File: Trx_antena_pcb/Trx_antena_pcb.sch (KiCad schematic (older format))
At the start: 3 parts

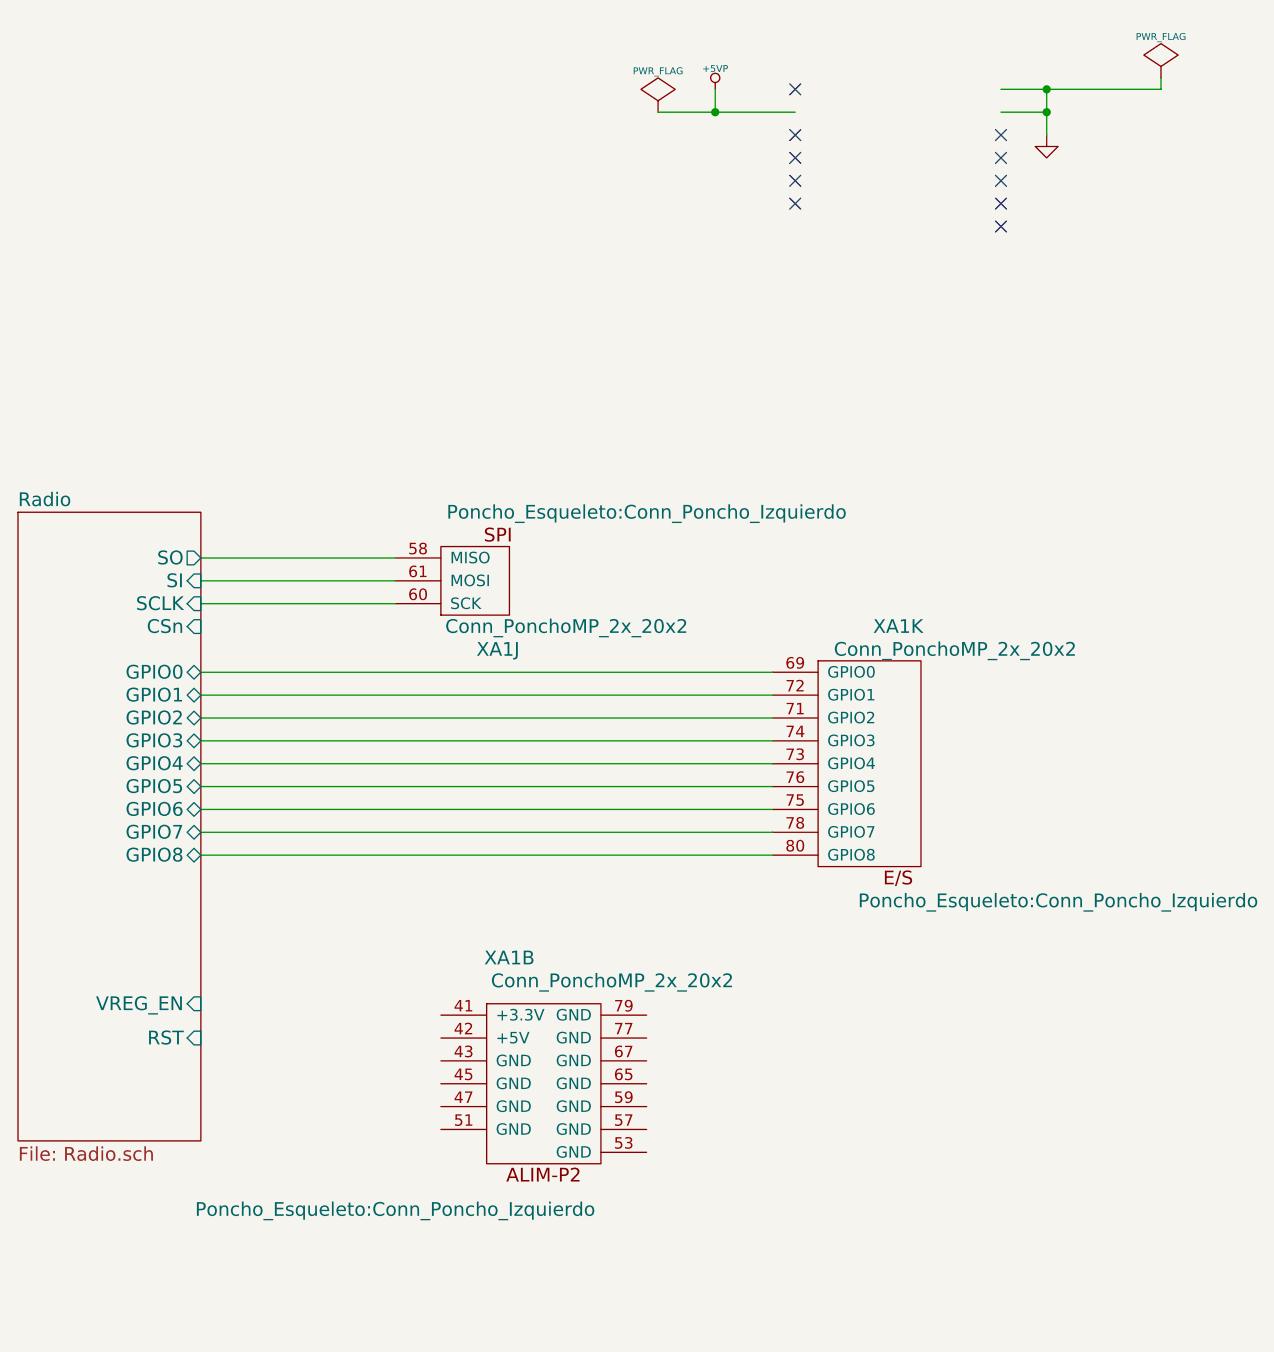
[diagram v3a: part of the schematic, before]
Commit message: completando el esquematico
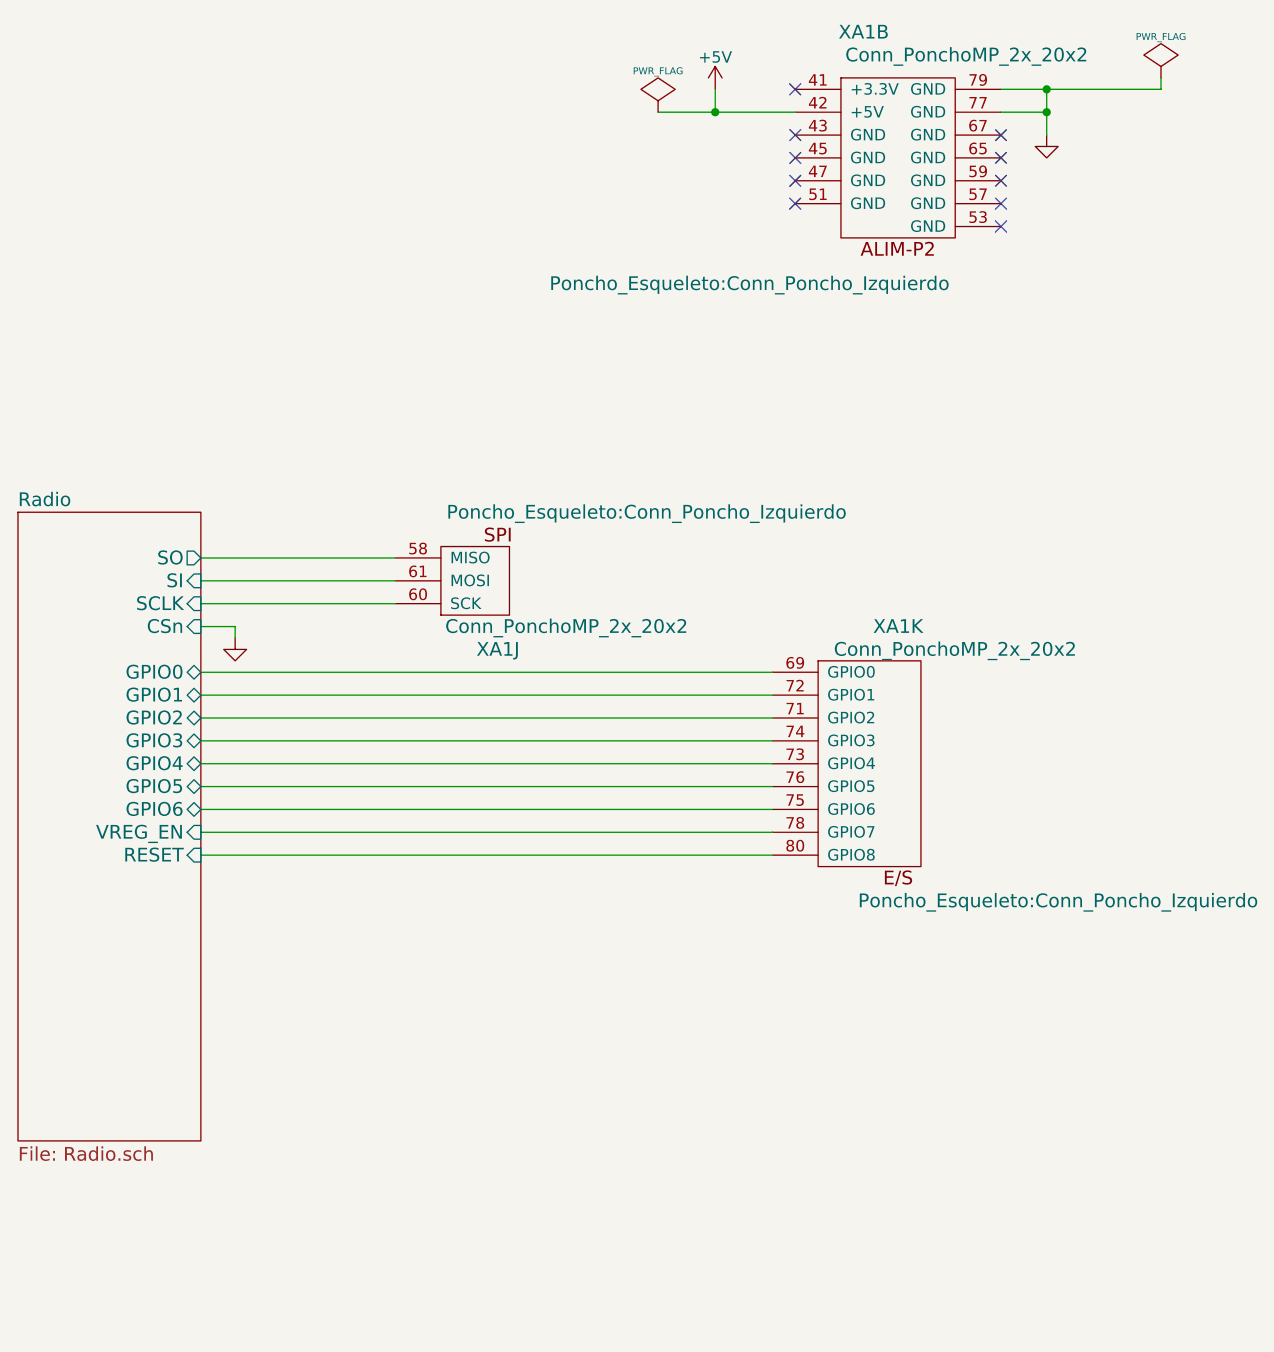
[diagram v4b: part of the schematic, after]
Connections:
- net labels added: +5V
- net labels removed: +5VP
- wire segments 18 -> 20
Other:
- moved on the sheet: XA1B
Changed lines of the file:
@@
 $EndComp
 $Comp
-L PWR_FLAG #FLG1
+L PWR_FLAG #FLG01
 U 1 1 560EE826
 P 3750 1050
-F 0 "#FLG1" H 3750 1145 30  0001 C CNN
+F 0 "#FLG01" H 3750 1145 30  0001 C CNN
 F 1 "PWR_FLAG" H 3750 1230 30  0000 C CNN
 F 2 "" H 3750 1050 60  0000 C CNN
@@
 $EndComp
 $Comp
-L +5VP #PWR2
-U 1 1 560EE7D3
-P 4000 950
-F 0 "#PWR2" H 4000 1040 20  0001 C CNN
-F 1 "+5VP" H 4000 1040 30  0000 C CNN
-F 2 "" H 4000 950 60  0000 C CNN
-F 3 "" H 4000 950 60  0000 C CNN
-	1    4000 950
-	1    0    0    -1
-$EndComp
-$Comp
-L GND #PWR5
+L GND #PWR02
 U 1 1 560EE345
 P 5450 1150
-F 0 "#PWR5" H 5450 1150 30  0001 C CNN
+F 0 "#PWR02" H 5450 1150 30  0001 C CNN
 F 1 "GND" H 5450 1080 30  0001 C CNN
 F 2 "" H 5450 1150 60  0000 C CNN
@@
 L Conn_PonchoMP_2x_20x2 XA1
 U 2 1 560EE110
-P 3250 5300
-F 0 "XA1" H 3100 5850 60  0000 C CNN
-F 1 "Conn_PonchoMP_2x_20x2" H 3550 5750 60  0000 C CNN
-F 2 "Poncho_Esqueleto:Conn_Poncho_Izquierdo" H 2600 4750 60  0000 C CNN
-F 3 "" H 3100 5650 60  0000 C CNN
-	2    3250 5300
+P 4800 1250
+F 0 "XA1" H 4650 1800 60  0000 C CNN
+F 1 "Conn_PonchoMP_2x_20x2" H 5100 1700 60  0000 C CNN
+F 2 "Poncho_Esqueleto:Conn_Poncho_Izquierdo" H 4150 700 60  0000 C CNN
+F 3 "" H 4650 1600 60  0000 C CNN
+	2    4800 1250
 	1    0    0    -1
 $EndComp
 $Comp
-L PWR_FLAG #FLG2
+L PWR_FLAG #FLG03
 U 1 1 560EDE73
 P 5950 900
-F 0 "#FLG2" H 5950 995 30  0001 C CNN
+F 0 "#FLG03" H 5950 995 30  0001 C CNN
 F 1 "PWR_FLAG" H 5950 1080 30  0000 C CNN
 F 2 "" H 5950 900 60  0000 C CNN
@@
 Text Notes 7450 5650 0    60   ~ 0
 Agujeros para visualización de LEDs
-$Sheet
-S 950  2800 800  2750
-U 582F8126
-F0 "Radio" 60
-F1 "Radio.sch" 60
-F2 "SO" O R 1750 3000 60
-F3 "SI" I R 1750 3100 60
-F4 "VREG_EN" I R 1750 4950 60
-F5 "SCLK" I R 1750 3200 60
-F6 "GPIO0" B R 1750 3500 60
-F7 "GPIO1" B R 1750 3600 60
-F8 "GPIO2" B R 1750 3700 60
-F9 "GPIO3" B R 1750 3800 60
-F10 "GPIO4" B R 1750 3900 60
-F11 "GPIO5" B R 1750 4000 60
-F12 "RST" I R 1750 5100 60
-F13 "CSn" I R 1750 3300 60
-F14 "GPIO6" B R 1750 4100 60
-F15 "GPIO7" B R 1750 4200 60
-F16 "GPIO8" B R 1750 4300 60
-$EndSheet
 Connection ~ 4000 1050
 Wire Wire Line
@@
 Wire Wire Line
 	1750 4100 4250 4100
+$Sheet
+S 950  2800 800  2750
+U 582F8126
+F0 "Radio" 60
+F1 "Radio.sch" 60
+F2 "SO" O R 1750 3000 60
+F3 "SI" I R 1750 3100 60
+F4 "VREG_EN" I R 1750 4200 60
+F5 "SCLK" I R 1750 3200 60
+F6 "GPIO0" B R 1750 3500 60
+F7 "GPIO1" B R 1750 3600 60
+F8 "GPIO2" B R 1750 3700 60
+F9 "GPIO3" B R 1750 3800 60
+F10 "GPIO4" B R 1750 3900 60
+F11 "GPIO5" B R 1750 4000 60
+F12 "CSn" I R 1750 3300 60
+F13 "GPIO6" B R 1750 4100 60
+F14 "RESET" I R 1750 4300 60
+$EndSheet
 Wire Wire Line
-	1750 4200 4250 4200
+	4250 4200 1750 4200
+$Comp
+L +5V #PWR04
+U 1 1 5851A27B
+P 4000 950
+F 0 "#PWR04" H 4000 800 50  0001 C CNN
+F 1 "+5V" H 4000 1090 50  0000 C CNN
+F 2 "" H 4000 950 50  0000 C CNN
+F 3 "" H 4000 950 50  0000 C CNN
+	1    4000 950
+	1    0    0    -1
+$EndComp
 Wire Wire Line
-	1750 4300 4250 4300
+	4250 4300 1750 4300
+$Comp
+L GND #PWR05
+U 1 1 5852BF25
+P 1900 3350
+F 0 "#PWR05" H 1900 3350 30  0001 C CNN
+F 1 "GND" H 1900 3280 30  0001 C CNN
+F 2 "" H 1900 3350 60  0000 C CNN
+F 3 "" H 1900 3350 60  0000 C CNN
+	1    1900 3350
+	1    0    0    -1
+$EndComp
+Wire Wire Line
+	1900 3350 1900 3300
+Wire Wire Line
+	1900 3300 1750 3300
 $EndSCHEMATC

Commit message: cuarta correccion: revision2 en /doc
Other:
- note added: "Este circuito de poncho implementa una unidad de radio \nque opera en la banda de frecuencias abierta de 2.4GHz \ny compila con aplicaciones de la EDU-CIAA NXP \nque soportan el estándar IEEE 802.15.4: IEEE Standards Association. \nIEEE Standard for Local and metropolitan area networks–Part 15.4: \nLow-Rate Wireless Personal Area Networks (LR-WPANs) y ZIGBEE.\n\n2.4 GHz Antena(DN007): Inverted-F 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"
- note removed: "Este diseño puede copiarse como un \nTemplate de KICAD. \n1)En el administrador de Proyectos: \n Proyecto Nuevo -> Nuevo Proyecto desde Template\n2)Ingresar el nombre del poncho a crear.\n3)Indicar el directorio de este modelo."
- note removed: "Luego de abrir el nuevo proyecto:\n1)Editar datos del rótulo.\n2)Editar los archivos del subdirectorio "doc".\n2.1) Agregarse en el archivo de licencia.\n2.2) Colocar info mínima del Poncho en el LEEME.txt\n2.3) Colocar info mínima en el CAMBIOS.doc"
- moved on the sheet: XA1B, XA1J, XA1K
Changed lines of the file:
@@
 EESchema Schematic File Version 2
-LIBS:device
+LIBS:power
 LIBS:Trx_antena_pcb-cache
 EELAYER 25 0
@@
 Comment1 "https://github.com/ciaa/Ponchos/tree/master/modelos/doc"
 Comment2 "Basado en el template de Diego Brengi - UNLaM"
-Comment3 "Autor y Licencia del poncho (Juan Vicente Montilla-FIUBA). Ver directorio \"doc\""
-Comment4 "https://github.com/Juanvmont/Poncho-EDU-CIAA-NXP-RF-2.4GHz-Antena-PCB.git"
+Comment3 "Revisor designado (Esp. Ing. Patricio Bos-FIUBA)."
+Comment4 "Autor y Licencia del poncho (Esp. Ing. Juan Vicente Montilla-FIUBA). Ver directorio \"doc\""
 $EndDescr
 $Comp
@@
 	1    0    0    -1
 $EndComp
-Text Notes 6950 2850 0    79   Italic 16
-Este diseño puede copiarse como un \nTemplate de KICAD. \n1)En el administrador de Proyectos:  \n   Proyecto Nuevo -> Nuevo Proyecto desde Template\n2)Ingresar el nombre del poncho a crear.\n3)Indicar el directorio de este modelo.
-Text Notes 7000 1800 0    118  ~ 24
+Text Notes 7800 900  0    118  ~ 24
 http://www.proyecto-ciaa.com.ar/
 $Comp
 L Conn_PonchoMP_2x_20x2 XA1
 U 11 1 560E5596
-P 4700 3800
-F 0 "XA1" H 4600 4300 60  0000 C CNN
-F 1 "Conn_PonchoMP_2x_20x2" H 4350 4200 60  0000 C CNN
-F 2 "Poncho_Esqueleto:Conn_Poncho_Izquierdo" H 3900 3100 60  0000 C CNN
-F 3 "" H 4550 4150 60  0000 C CNN
-	11   4700 3800
+P 7100 2700
+F 0 "XA1" H 7000 3200 60  0000 C CNN
+F 1 "Conn_PonchoMP_2x_20x2" H 6750 3100 60  0000 C CNN
+F 2 "Poncho_Esqueleto:Conn_Poncho_Izquierdo" H 6300 2000 60  0001 C CNN
+F 3 "" H 6950 3050 60  0000 C CNN
+	11   7100 2700
 	-1   0    0    -1
 $EndComp
-Text Notes 7000 3950 0    60   ~ 0
-Luego de abrir el nuevo proyecto:\n1)Editar datos del rótulo.\n2)Editar los archivos del subdirectorio "doc".\n2.1) Agregarse en el archivo de licencia.\n2.2) Colocar info mínima del Poncho en el LEEME.txt\n2.3) Colocar info mínima en el CAMBIOS.doc
 $Comp
 L Conn_PonchoMP_2x_20x2 XA1
 U 10 1 560E54EF
-P 2950 3100
-F 0 "XA1" H 2850 3400 60  0000 C CNN
-F 1 "Conn_PonchoMP_2x_20x2" H 2550 3300 60  0000 C CNN
-F 2 "Poncho_Esqueleto:Conn_Poncho_Izquierdo" H 2200 2800 60  0000 C CNN
-F 3 "" H 2800 3450 60  0000 C CNN
-	10   2950 3100
+P 5350 2000
+F 0 "XA1" H 5250 2300 60  0000 C CNN
+F 1 "Conn_PonchoMP_2x_20x2" H 4950 2200 60  0000 C CNN
+F 2 "Poncho_Esqueleto:Conn_Poncho_Izquierdo" H 4600 1700 60  0001 C CNN
+F 3 "" H 5200 2350 60  0000 C CNN
+	10   5350 2000
 	-1   0    0    1
 $EndComp
@@
 L PWR_FLAG #FLG01
 U 1 1 560EE826
-P 3750 1050
-F 0 "#FLG01" H 3750 1145 30  0001 C CNN
-F 1 "PWR_FLAG" H 3750 1230 30  0000 C CNN
-F 2 "" H 3750 1050 60  0000 C CNN
-F 3 "" H 3750 1050 60  0000 C CNN
-	1    3750 1050
+P 5100 4350
+F 0 "#FLG01" H 5100 4445 30  0001 C CNN
+F 1 "PWR_FLAG" H 5100 4530 30  0000 C CNN
+F 2 "" H 5100 4350 60  0000 C CNN
+F 3 "" H 5100 4350 60  0000 C CNN
+	1    5100 4350
 	1    0    0    -1
 $EndComp
@@
 L GND #PWR02
 U 1 1 560EE345
-P 5450 1150
-F 0 "#PWR02" H 5450 1150 30  0001 C CNN
-F 1 "GND" H 5450 1080 30  0001 C CNN
-F 2 "" H 5450 1150 60  0000 C CNN
-F 3 "" H 5450 1150 60  0000 C CNN
-	1    5450 1150
-	1    0    0    -1
-$EndComp
-NoConn ~ 5250 1150
-NoConn ~ 5250 1250
-NoConn ~ 5250 1350
-NoConn ~ 5250 1450
-NoConn ~ 5250 1550
-NoConn ~ 4350 1450
-NoConn ~ 4350 950
+P 6800 4450
+F 0 "#PWR02" H 6800 4450 30  0001 C CNN
+F 1 "GND" H 6800 4380 30  0001 C CNN
+F 2 "" H 6800 4450 60  0000 C CNN
+F 3 "" H 6800 4450 60  0000 C CNN
+	1    6800 4450
+	1    0    0    -1
+$EndComp
+NoConn ~ 6600 4450
+NoConn ~ 6600 4550
+NoConn ~ 6600 4650
+NoConn ~ 6600 4750
+NoConn ~ 6600 4850
+NoConn ~ 5700 4750
+NoConn ~ 5700 4250
 $Comp
 L Conn_PonchoMP_2x_20x2 XA1
 U 2 1 560EE110
-P 4800 1250
-F 0 "XA1" H 4650 1800 60  0000 C CNN
-F 1 "Conn_PonchoMP_2x_20x2" H 5100 1700 60  0000 C CNN
-F 2 "Poncho_Esqueleto:Conn_Poncho_Izquierdo" H 4150 700 60  0000 C CNN
-F 3 "" H 4650 1600 60  0000 C CNN
-	2    4800 1250
+P 6150 4550
+F 0 "XA1" H 6000 5100 60  0000 C CNN
+F 1 "Conn_PonchoMP_2x_20x2" H 6450 5000 60  0000 C CNN
+F 2 "Poncho_Esqueleto:Conn_Poncho_Izquierdo" H 5500 4000 60  0001 C CNN
+F 3 "" H 6000 4900 60  0000 C CNN
+	2    6150 4550
 	1    0    0    -1
 $EndComp
@@
 L PWR_FLAG #FLG03
 U 1 1 560EDE73
-P 5950 900
-F 0 "#FLG03" H 5950 995 30  0001 C CNN
-F 1 "PWR_FLAG" H 5950 1080 30  0000 C CNN
-F 2 "" H 5950 900 60  0000 C CNN
-F 3 "" H 5950 900 60  0000 C CNN
-	1    5950 900
-	1    0    0    -1
-$EndComp
-NoConn ~ 4350 1350
-NoConn ~ 4350 1250
-NoConn ~ 4350 1150
+P 7300 4200
+F 0 "#FLG03" H 7300 4295 30  0001 C CNN
+F 1 "PWR_FLAG" H 7300 4380 30  0000 C CNN
+F 2 "" H 7300 4200 60  0000 C CNN
+F 3 "" H 7300 4200 60  0000 C CNN
+	1    7300 4200
+	1    0    0    -1
+$EndComp
+NoConn ~ 5700 4650
+NoConn ~ 5700 4550
+NoConn ~ 5700 4450
 $Comp
 L PCB_HOLE H2
@@
 Text Notes 7450 5650 0    60   ~ 0
 Agujeros para visualización de LEDs
-Connection ~ 4000 1050
-Wire Wire Line
-	4000 1050 4000 950
-Wire Wire Line
-	3750 1050 4350 1050
-Connection ~ 5450 1050
-Wire Wire Line
-	5250 950  5950 950
-Wire Wire Line
-	5450 950  5450 1150
-Wire Wire Line
-	5250 1050 5450 1050
-Wire Wire Line
-	5950 950  5950 900
-Connection ~ 5450 950
-Wire Wire Line
-	2600 3000 1750 3000
-Wire Wire Line
-	2600 3100 1750 3100
-Wire Wire Line
-	2600 3200 1750 3200
-Wire Wire Line
-	1750 3500 4250 3500
-Wire Wire Line
-	4250 3600 1750 3600
-Wire Wire Line
-	1750 3700 4250 3700
-Wire Wire Line
-	1750 3800 4250 3800
-Wire Wire Line
-	1750 3900 4250 3900
-Wire Wire Line
-	1750 4000 4250 4000
-Wire Wire Line
-	1750 4100 4250 4100
+Connection ~ 5350 4350
+Wire Wire Line
+	5350 4350 5350 4250
+Wire Wire Line
+	5100 4350 5700 4350
+Connection ~ 6800 4350
+Wire Wire Line
+	6600 4250 7300 4250
+Wire Wire Line
+	6800 4250 6800 4450
+Wire Wire Line
+	6600 4350 6800 4350
+Wire Wire Line
+	7300 4250 7300 4200
+Connection ~ 6800 4250
+Wire Wire Line
+	5000 1900 4150 1900
+Wire Wire Line
+	5000 2000 4150 2000
+Wire Wire Line
+	5000 2100 4150 2100
+Wire Wire Line
+	4150 2400 6650 2400
+Wire Wire Line
+	6650 2500 4150 2500
+Wire Wire Line
+	4150 2600 6650 2600
+Wire Wire Line
+	4150 2700 6650 2700
+Wire Wire Line
+	4150 2800 6650 2800
+Wire Wire Line
+	4150 2900 6650 2900
+Wire Wire Line
+	4150 3000 6650 3000
 $Sheet
-S 950  2800 800  2750
+S 3350 1700 800  2750
 U 582F8126
 F0 "Radio" 60
 F1 "Radio.sch" 60
-F2 "SO" O R 1750 3000 60
-F3 "SI" I R 1750 3100 60
-F4 "VREG_EN" I R 1750 4200 60
-F5 "SCLK" I R 1750 3200 60
-F6 "GPIO0" B R 1750 3500 60
-F7 "GPIO1" B R 1750 3600 60
-F8 "GPIO2" B R 1750 3700 60
-F9 "GPIO3" B R 1750 3800 60
-F10 "GPIO4" B R 1750 3900 60
-F11 "GPIO5" B R 1750 4000 60
-F12 "CSn" I R 1750 3300 60
-F13 "GPIO6" B R 1750 4100 60
-F14 "RESET" I R 1750 4300 60
+F2 "SO" O R 4150 1900 60
+F3 "SI" I R 4150 2000 60
+F4 "VREG_EN" I R 4150 3100 60
+F5 "SCLK" I R 4150 2100 60
+F6 "GPIO0" B R 4150 2400 60
+F7 "GPIO1" B R 4150 2500 60
+F8 "GPIO2" B R 4150 2600 60
+F9 "GPIO3" B R 4150 2700 60
+F10 "GPIO4" B R 4150 2800 60
+F11 "GPIO5" B R 4150 2900 60
+F12 "CSn" I R 4150 2200 60
+F13 "GPIO6" B R 4150 3000 60
+F14 "RESET" I R 4150 3200 60
 $EndSheet
 Wire Wire Line
-	4250 4200 1750 4200
+	6650 3100 4150 3100
 $Comp
 L +5V #PWR04
 U 1 1 5851A27B
-P 4000 950
-F 0 "#PWR04" H 4000 800 50  0001 C CNN
-F 1 "+5V" H 4000 1090 50  0000 C CNN
-F 2 "" H 4000 950 50  0000 C CNN
-F 3 "" H 4000 950 50  0000 C CNN
-	1    4000 950
-	1    0    0    -1
-$EndComp
-Wire Wire Line
-	4250 4300 1750 4300
+P 5350 4250
+F 0 "#PWR04" H 5350 4100 50  0001 C CNN
+F 1 "+5V" H 5350 4390 50  0000 C CNN
+F 2 "" H 5350 4250 50  0000 C CNN
+F 3 "" H 5350 4250 50  0000 C CNN
+	1    5350 4250
+	1    0    0    -1
+$EndComp
+Wire Wire Line
+	6650 3200 4150 3200
 $Comp
 L GND #PWR05
 U 1 1 5852BF25
-P 1900 3350
-F 0 "#PWR05" H 1900 3350 30  0001 C CNN
-F 1 "GND" H 1900 3280 30  0001 C CNN
-F 2 "" H 1900 3350 60  0000 C CNN
-F 3 "" H 1900 3350 60  0000 C CNN
-	1    1900 3350
-	1    0    0    -1
-$EndComp
-Wire Wire Line
-	1900 3350 1900 3300
-Wire Wire Line
-	1900 3300 1750 3300
+P 4300 2250
+F 0 "#PWR05" H 4300 2250 30  0001 C CNN
+F 1 "GND" H 4300 2180 30  0001 C CNN
+F 2 "" H 4300 2250 60  0000 C CNN
+F 3 "" H 4300 2250 60  0000 C CNN
+	1    4300 2250
+	1    0    0    -1
+$EndComp
+Wire Wire Line
+	4300 2250 4300 2200
+Wire Wire Line
+	4300 2200 4150 2200
+Text Notes 1000 7200 0    60   ~ 0
+Este circuito de poncho implementa una unidad de radio \nque opera en la banda de frecuencias abierta de 2.4GHz \ny compila con aplicaciones de la EDU-CIAA NXP \nque soportan el estándar IEEE 802.15.4: IEEE Standards Association. \nIEEE Standard for Local and metropolitan area networks–Part 15.4: \nLow-Rate Wireless Personal Area Networks (LR-WPANs) y ZIGBEE.\n\n2.4 GHz Antena(DN007): Inverted-F Antenna (IFA) \nGanancia en plano XY: 1.1 dB\nGanancia en plano XZ: 3.3 dB\nGanancia en plano YZ: 1.6 dB\nGanancia máxima: +3.3 dB\nEficiencia típica: 80% (EB) 94% (SA)\nAncho de banda @ VSWR 2.0: 280 MHz\nDimensiones (mm): 26 x 8\nReflexión: < -15 dB  (<10% de la potencia disponible para un ancho de banda  de >300MHz)\n\nGuía de Selección de Antena. Texas Instrument.   http://www.ti.com/lit/an/swra161b/swra161b.pdf\nDesign Note DN0007: 2.4 GHz Inverted F Antenna http://www.ti.com/lit/an/swru120b/swru120b.pdf\nReference Design: Using CC2591 Front End with CC2520\nhttp://www.ti.com/lit/an/swra229a/swra229a.pdf
 $EndSCHEMATC
